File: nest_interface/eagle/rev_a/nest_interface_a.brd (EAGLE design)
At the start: 50.8 x 50.8 mm, 87 parts, among them J1 MOLEX_MICRO_USB_B_047346, J10 CONN_BLOCK_2, J11 CONN_BLOCK_2, J12 CONN_BLOCK_2, J13 CONN_BLOCK_2, J14 CONN_BLOCK_2, J15 CONN_BLOCK_2, J2 CONN_BLOCK_2, J3 CONN_BLOCK_3, J4 PJ-036A-SMT, J5 CONN_BLOCK_3, J6 CONN_BLOCK_3, J7 CONN_BLOCK_2, J8 CONN_BLOCK_3, J9 CONN_BLOCK_3, U1 FT232RL, U2 EPIC-CORE_A

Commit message: started routing the nest interface board
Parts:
- added JP1: (no value), pinhead:2X10
- moved R13 349.9 mm to (45.7, 50.8), turned to 180 degrees
- moved R12 337.4 mm to (45.7, 34.3), turned to 180 degrees
- moved C11 336.6 mm to (45.7, 47.0), turned to 180 degrees
- moved RE6 324.6 mm to (27.9, 45.7)
- moved C10 322.9 mm to (45.7, 30.5), turned to 180 degrees
- moved C9 302.6 mm to (45.7, 12.7), turned to 180 degrees
- moved RE5 292.7 mm to (27.9, 29.2)
- moved R11 291.5 mm to (45.7, 16.5), turned to 180 degrees
- moved RE4 260.2 mm to (27.9, 11.4)
- moved U2 178.7 mm to (74.9, 26.7), turned to 270 degrees
- moved J1 155.3 mm to (58.4, 55.9)
- moved J4 25.4 mm to (17.1, 69.2)
- moved J2 14.0 mm to (3.81, 52.1)
- moved J3 12.7 mm to (3.81, 42.5)
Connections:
- new net ADC5: JP1.1, U2.P$24
- new net ADC6/DAC0: JP1.3, U2.P$25
- new net ADC7/DAC1: JP1.5, U2.P$26
- new net MISO0: JP1.11, U2.P$57
- new net MOSI0/SDA: JP1.9, U2.P$56
- new net P2.0: JP1.2, U2.P$38
- new net P2.1: JP1.4, U2.P$39
- new net P2.3: JP1.6, U2.P$40
- new net P2.6: JP1.8, U2.P$41
- new net RADIO_SFD: JP1.10, U2.P$50
- new net SCLK0/SCL: JP1.13, U2.P$58
- new net STE0: JP1.7, U2.P$55
- new net UART0RX: JP1.17, U2.P$60
- new net UART0TX: JP1.15, U2.P$59
- net FAN_PIN: now also U2.P$31; no longer U2.P$33
- net HEATING_PIN: now also U2.P$33; no longer U2.P$31
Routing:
- net COMMON: track 0.00 -> 71.6 mm
- net W: track 0.00 -> 37.1 mm
- net HEATING_PIN: track 0.00 -> 23.9 mm
- net COOLING_PIN: track 0.00 -> 23.9 mm
- net FAN_PIN: track 0.00 -> 23.9 mm
- net Y: track 0.00 -> 23.7 mm
- net RH: track 0.00 -> 16.5 mm
- net G: track 0.00 -> 12.8 mm
- added copper zone on layer 16, net GND
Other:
- board size 50.8 x 50.8 mm -> 101.6 x 76.2 mm

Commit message: routed the nest interface board
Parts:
- moved J15 472.5 mm to (56.6, 72.4), turned to 180 degrees
- moved J14 467.6 mm to (63.5, 72.4), turned to 180 degrees
- moved JP1 467.1 mm to (64.8, 58.4)
- moved J13 463.7 mm to (72.4, 72.4), turned to 180 degrees
- moved J12 459.2 mm to (79.2, 72.4), turned to 180 degrees
- moved Q8 418.0 mm to (92.7, 30.5), turned to 270 degrees
- moved Q9 412.5 mm to (92.7, 26.2), turned to 270 degrees
- moved Q10 406.9 mm to (92.7, 21.8), turned to 270 degrees
- moved Q6 404.5 mm to (92.7, 40.6), turned to 270 degrees
- moved R23 403.6 mm to (85.9, 30.5), turned to 90 degrees
- moved Q13 403.4 mm to (92.7, 8.89), turned to 270 degrees
- moved Q11 401.3 mm to (92.7, 17.5), turned to 270 degrees
- moved Q5 399.7 mm to (92.7, 45.0), turned to 270 degrees
- moved R29 399.5 mm to (85.9, 17.5), turned to 90 degrees
- moved Q7 398.9 mm to (92.7, 36.3), turned to 270 degrees
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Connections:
- removed net TSTAT1_GND: J7.2
- removed net TSTAT2_GND: J10.2
- net ADC5: now also JP1.16; no longer JP1.1
- net ADC6/DAC0: now also JP1.14; no longer JP1.3
- net ADC7/DAC1: now also JP1.12; no longer JP1.5
- net GND: now also J10.1, J7.1
- net MISO0: now also JP1.13; no longer JP1.11
- net MOSI0/SDA: now also JP1.11; no longer JP1.9
- net P2.0: now also JP1.1; no longer JP1.2
- net P2.1: now also JP1.3; no longer JP1.4
- net P2.3: now also JP1.5; no longer JP1.6
- net P2.6: now also JP1.7; no longer JP1.8
- net SCLK0/SCL: now also JP1.15; no longer JP1.13
- net STE0: now also JP1.9; no longer JP1.7
- net TSTAT1_DOWN: now also J6.1; no longer J6.3
- net TSTAT1_DOWN_PIN: now also U2.P$4; no longer U2.P$7
- net TSTAT1_ENTER: now also J7.2; no longer J7.1
- net TSTAT1_ENTER_PIN: now also U2.P$3; no longer U2.P$8
- net TSTAT1_ESC: now also J6.3; no longer J6.1
- net TSTAT1_ESC_PIN: now also U2.P$6; no longer U2.P$5
- net TSTAT1_HELP_PIN: now also U2.P$5; no longer U2.P$6
- net TSTAT1_MENU_PIN: now also U2.P$8; no longer U2.P$3
- net TSTAT1_ON/OFF: now also J5.3; no longer J5.1
- net TSTAT1_ON/OFF_PIN: now also U2.P$9; no longer U2.P$2
- net TSTAT1_UP: now also J5.1; no longer J5.3
- net TSTAT1_UP_PIN: now also U2.P$7; no longer U2.P$4
- net TSTAT2_DOWN: now also J9.1; no longer J9.3
- net TSTAT2_ENTER: now also J10.2; no longer J10.1
- net TSTAT2_ESC: now also J9.3; no longer J9.1
- net TSTAT2_ON/OFF: now also J8.3; no longer J8.1
- net TSTAT2_ON/OFF_PIN: now also U2.P$2; no longer U2.P$9
- net TSTAT2_UP: now also J8.1; no longer J8.3
- net UART0RX: now also JP1.19; no longer JP1.17
- net UART0TX: now also JP1.17; no longer JP1.15
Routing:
- net VCC: track 0.00 -> 225.6 mm, vias 0 -> 9
- net GND: track 0.00 -> 102.8 mm, vias 0 -> 26
- net N$14: track 0.00 -> 66.3 mm, vias 0 -> 2
- net N$8: track 0.00 -> 65.0 mm
- net TSTAT2_ENTER_PIN: track 0.00 -> 59.0 mm, vias 0 -> 2
- net N$12: track 0.00 -> 56.0 mm, vias 0 -> 2
- net N$9: track 0.00 -> 53.9 mm, vias 0 -> 4
- net TSTAT2_DOWN_PIN: track 0.00 -> 50.9 mm, vias 0 -> 2
- net 5V: track 0.00 -> 49.8 mm
- net TSTAT2_HELP_PIN: track 0.00 -> 46.2 mm, vias 0 -> 2
- net HEATING_PIN: track 23.9 -> 70.0 mm
- net TSTAT2_ESC_PIN: track 0.00 -> 41.3 mm, vias 0 -> 2
- net RADIO_SFD: track 0.00 -> 39.6 mm, vias 0 -> 1
- net UART0RX: track 0.00 -> 37.1 mm, vias 0 -> 1
- net UART0TX: track 0.00 -> 36.6 mm, vias 0 -> 1
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- added copper zone on layer 1, net GND
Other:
- board size 101.6 x 76.2 mm -> 105.4 x 76.2 mm

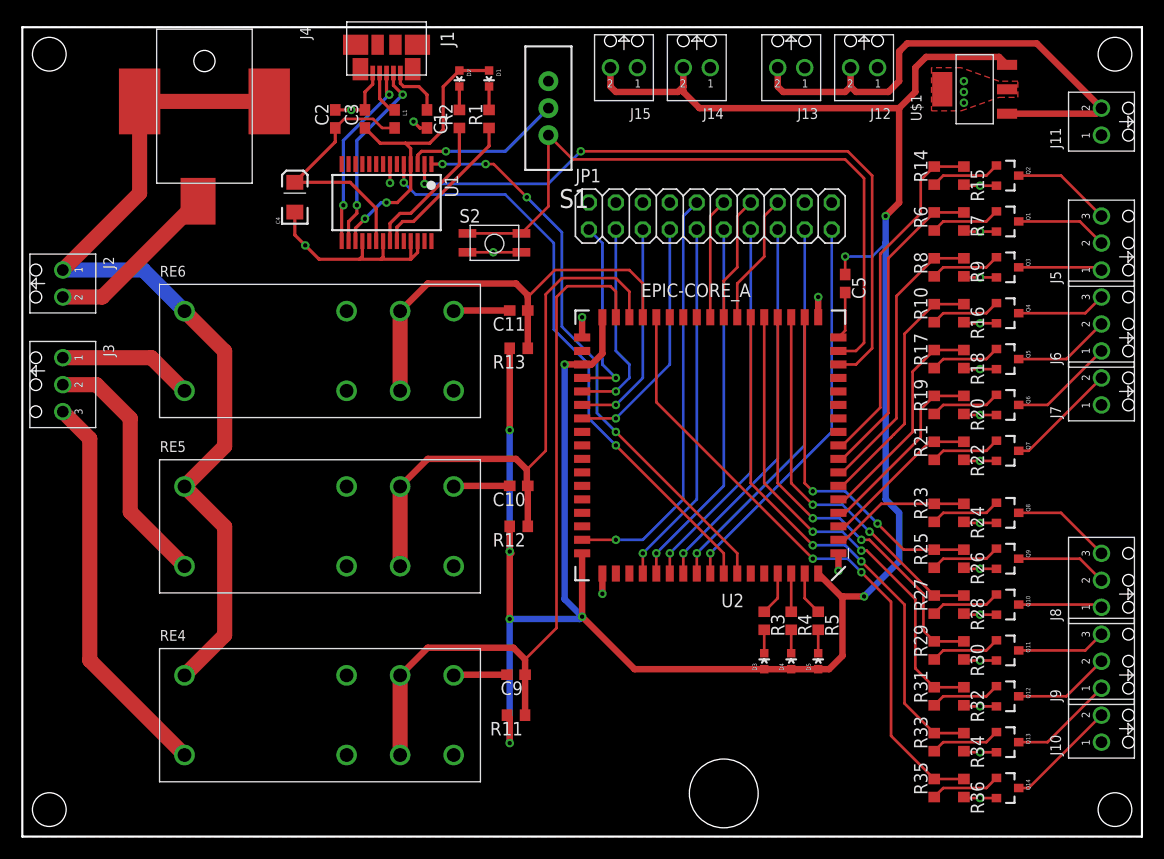
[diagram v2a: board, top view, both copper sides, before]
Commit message: added silkscreen to nest board
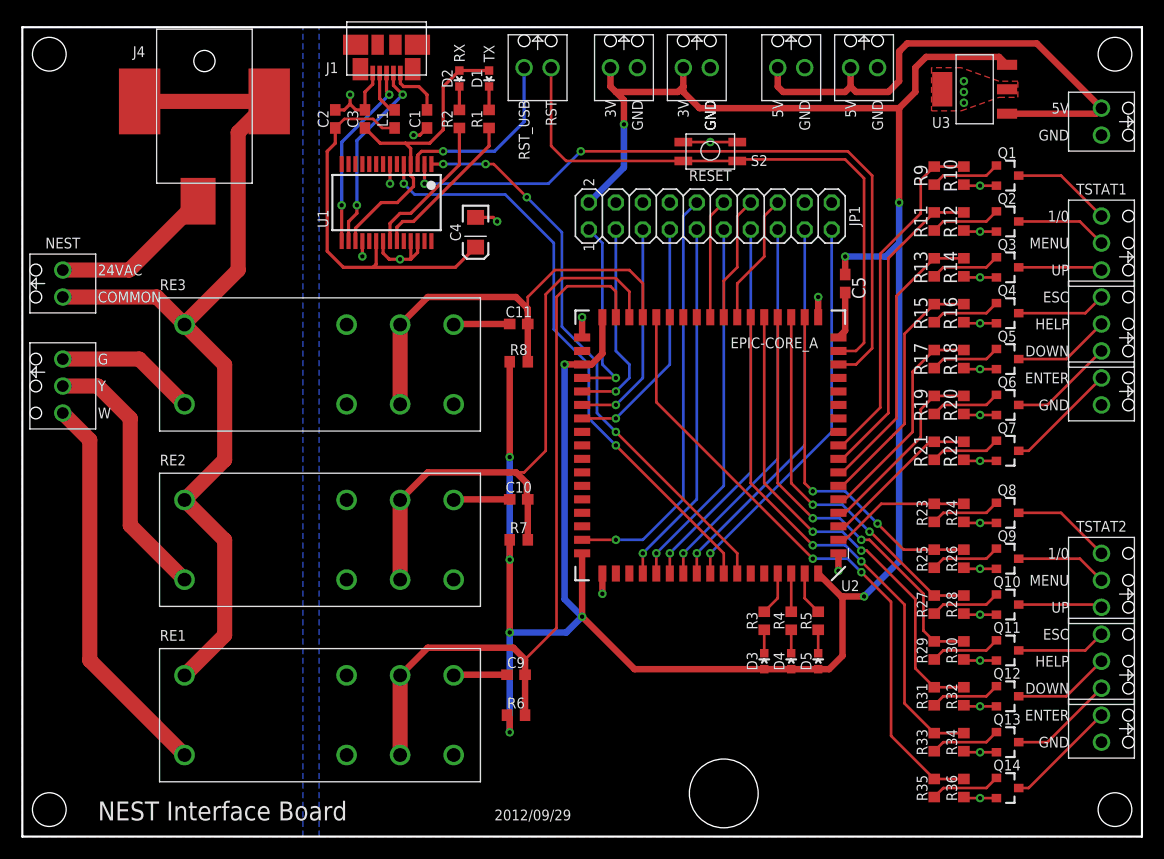
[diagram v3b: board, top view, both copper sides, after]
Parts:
- removed RE5, RE6: RT314524, nest_interface:S0418-CA
- removed S1: (no value), SparkFun:SWITCH-SPDT
- added J16: CONN_BLOCK_2, nest_interface:CONN_BLOCK_2
- added RE2, RE3: RT314524, nest_interface:S0418-CA
- R10, R14, R6, R8: value 10k -> 100k
- R11, R13, R15, R9: value 100k -> 10k
- moved R11 60.9 mm to (85.9, 57.9), turned to 90 degrees
- moved R6 60.9 mm to (46.5, 11.4), turned to 180 degrees
- moved R7 51.5 mm to (46.7, 27.9), turned to 180 degrees
- moved R12 50.8 mm to (88.6, 57.9), turned to 270 degrees
- moved R8 40.1 mm to (46.7, 44.7), turned to 180 degrees
- moved R13 39.9 mm to (85.9, 53.6), turned to 90 degrees
- moved S2 22.1 mm to (64.8, 64.5), turned to 180 degrees
- moved C4 17.3 mm to (42.7, 56.9), turned to 270 degrees
- moved R10 13.3 mm to (88.6, 62.2), turned to 270 degrees
- moved R15 13.3 mm to (85.9, 49.3), turned to 90 degrees
- moved R14 9.08 mm to (88.6, 53.6), turned to 270 degrees
- moved R9 9.08 mm to (85.9, 62.2), turned to 90 degrees
- moved Q1 4.32 mm to (92.7, 62.2)
- moved Q2 4.32 mm to (92.7, 57.9)
- moved C10 1.27 mm to (46.7, 31.8)
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- renumbered RE4 to RE1, U$1 to U3
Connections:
- removed net N$13: S1.2, U1.3
- removed net N$8: S1.1, S2.P$2, S2.P$4, U2.P$16
- new net RST: J16.1, S2.P$2, S2.P$4, U2.P$16
- new net RST_USB: J16.2, U1.3
- net COMMON: now also J2.2, RE2.A2, RE3.A2; no longer J2.1, RE5.A2, RE6.A2
- net COOLING_PIN: now also R7.1, RE2.COMMON1, RE2.COMMON2; no longer R12.1, RE5.COMMON1, RE5.COMMON2
- net FAN_PIN: now also R8.1, RE3.COMMON1, RE3.COMMON2; no longer R13.1, RE6.COMMON1, RE6.COMMON2
- net G: now also RE3.A1; no longer RE6.A1
- net GND: now also JP1.20, R10.2, R12.2, R14.2, RE2.NO1, RE2.NO2, RE3.NO1, RE3.NO2; no longer R15.2, R7.2, R9.2, RE5.NO1, RE5.NO2, RE6.NO1, RE6.NO2
- net HEATING_PIN: now also R6.1; no longer R11.1
- net N$16: now also Q2.1, R11.1; no longer Q1.1, R6.1
- net N$17: now also Q1.1, R9.1; no longer Q2.1, R14.1
- net N$25: now also R13.1; no longer R8.1
- net N$26: now also R15.1; no longer R10.1
- net RH: now also J2.1; no longer J2.2
- net TSTAT1_ESC_PIN: now also R15.2; no longer R10.2
- net TSTAT1_MENU: now also Q2.3; no longer Q1.3
- net TSTAT1_MENU_PIN: now also R11.2, R12.1; no longer R6.2, R7.1
- net TSTAT1_ON/OFF: now also Q1.3; no longer Q2.3
- net TSTAT1_ON/OFF_PIN: now also R10.1, R9.2; no longer R14.2, R15.1
- net TSTAT1_UP_PIN: now also R13.2, R14.1; no longer R8.2, R9.1
- net VCC: now also JP1.2, R6.2, R7.2, R8.2; no longer R11.2, R12.2, R13.2
- net Y: now also RE2.A1; no longer RE5.A1
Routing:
- net N$8: track 65.0 -> 0.00 mm
- net RST: track 0.00 -> 56.4 mm
- net RST_USB: track 0.00 -> 17.2 mm, vias 0 -> 1
- net N$13: track 15.0 -> 0.00 mm, vias 1 -> 0
- net N$6: track 24.7 -> 36.2 mm
- net VCC: track 225.6 -> 234.4 mm, vias 9 -> 10
- net GND: track 102.8 -> 94.2 mm, vias 26 -> 28
- net COMMON: track 84.7 -> 88.3 mm
- net COOLING_PIN: track 55.0 -> 56.9 mm
- net FAN_PIN: track 41.6 -> 42.9 mm
- net Y: track 23.7 -> 24.9 mm
- net RH: track 16.5 -> 15.4 mm
- net N$15: track 30.0 -> 30.2 mm, vias 2 -> 0
- added copper zone on layer 16, net N$37
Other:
- board text added: "1"
- board text added: "1/0"
- board text added: "2"
- board text added: "2012/09/29"
- board text added: "24VAC"
- board text added: "3V"
- board text added: "5V"
- board text added: "COMMON"
- board text added: "DOWN"
- board text added: "ENTER"
- board text added: "ESC"
- board text added: "G"
- board text added: "GND"
- board text added: "HELP"
- board text added: "MENU"
- board text added: "NEST"
- board text added: "NEST Interface Board"
- board text added: "RESET"
- board text added: "RST"
- board text added: "RST_USB"
- board text added: "RX"
- board text added: "TSTAT1"
- board text added: "TSTAT2"
- board text added: "TX"
- board text added: "UP"
- board text added: "W"
- board text added: "Y"

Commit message: tweaks to nest interface board
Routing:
- net GND: vias 28 -> 30
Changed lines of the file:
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@@
 <wire x1="88.746" y1="3.622" x2="90.17" y2="3.622" width="0.254" layer="1"/>
 <polygon width="0.254" layer="1">
-<vertex x="85.598" y="72.39"/>
-<vertex x="85.598" y="68.326"/>
+<vertex x="85.09" y="72.39"/>
+<vertex x="85.09" y="68.326"/>
 <vertex x="88.392" y="68.326"/>
-<vertex x="91.948" y="69.596"/>
-<vertex x="93.726" y="69.596"/>
-<vertex x="93.726" y="71.12"/>
-<vertex x="91.948" y="71.12"/>
+<vertex x="91.948" y="68.834"/>
+<vertex x="94.234" y="68.834"/>
+<vertex x="94.234" y="71.882"/>
+<vertex x="91.948" y="71.882"/>
 <vertex x="88.392" y="72.39"/>
 </polygon>
-<via x="88.646" y="71.12" extent="1-16" drill="0.4064"/>
-<via x="88.646" y="70.104" extent="1-16" drill="0.4064"/>
-<via x="88.646" y="69.088" extent="1-16" drill="0.4064"/>
+<via x="88.646" y="71.374" extent="1-16" drill="0.4064"/>
+<via x="88.646" y="70.358" extent="1-16" drill="0.4064"/>
+<via x="88.646" y="69.342" extent="1-16" drill="0.4064"/>
 <wire x1="54.61" y1="24.765" x2="54.61" y2="22.86" width="0.6096" layer="1"/>
 <via x="54.61" y="22.86" extent="1-16" drill="0.4064"/>
@@
 <wire x1="44.32" y1="58.296" x2="44.704" y2="57.912" width="0.3048" layer="1"/>
 <via x="44.704" y="57.912" extent="1-16" drill="0.4064"/>
+<via x="89.916" y="70.358" extent="1-16" drill="0.4064"/>
+<via x="91.186" y="70.358" extent="1-16" drill="0.4064"/>
 </signal>
 <signal name="N$1">
@@
 <contactref element="J13" pad="2"/>
 <wire x1="101.078" y1="68.058" x2="92.712" y2="68.058" width="0.6096" layer="1"/>
-<wire x1="95.504" y1="74.676" x2="83.312" y2="74.676" width="0.6096" layer="1"/>
 <wire x1="77.978" y1="70.612" x2="77.978" y2="72.39" width="0.6096" layer="1"/>
 <wire x1="71.12" y1="72.39" x2="71.12" y2="70.612" width="0.6096" layer="1"/>
@@
 <wire x1="78.486" y1="70.104" x2="81.534" y2="70.104" width="0.6096" layer="1"/>
 <wire x1="81.534" y1="70.104" x2="82.55" y2="71.12" width="0.6096" layer="1"/>
-<wire x1="82.55" y1="71.12" x2="82.55" y2="73.914" width="0.6096" layer="1"/>
-<wire x1="82.55" y1="73.914" x2="83.312" y2="74.676" width="0.6096" layer="1"/>
 <wire x1="101.078" y1="68.058" x2="101.6" y2="68.58" width="0.6096" layer="1"/>
-<wire x1="101.6" y1="68.58" x2="95.504" y2="74.676" width="0.6096" layer="1"/>
+<wire x1="101.6" y1="68.58" x2="101.6" y2="70.612" width="0.6096" layer="1"/>
+<wire x1="101.6" y1="70.612" x2="97.536" y2="74.676" width="0.6096" layer="1"/>
+<wire x1="97.536" y1="74.676" x2="84.582" y2="74.676" width="0.6096" layer="1"/>
+<wire x1="84.582" y1="74.676" x2="82.55" y2="72.644" width="0.6096" layer="1"/>
+<wire x1="82.55" y1="72.644" x2="82.55" y2="71.12" width="0.6096" layer="1"/>
 </signal>
 <signal name="TSTAT1_ON/OFF">

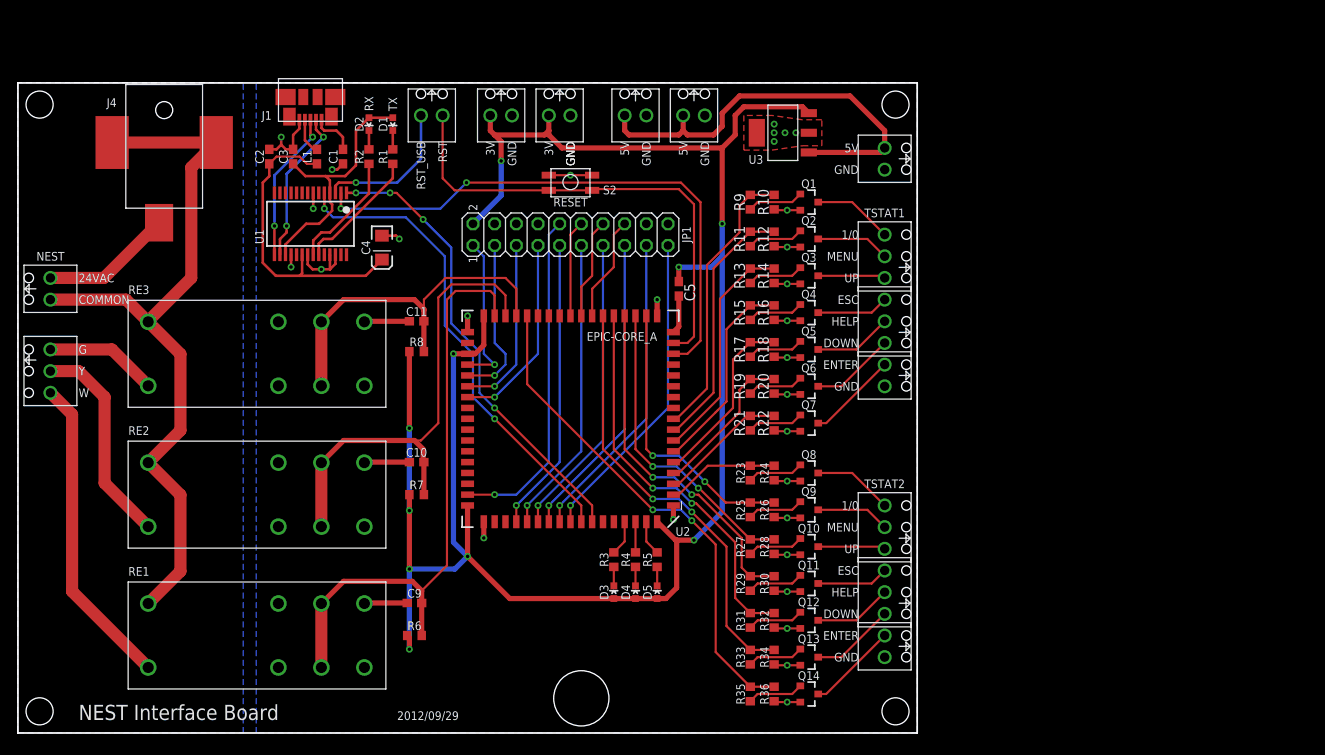
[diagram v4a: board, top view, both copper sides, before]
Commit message: adding more relays to the nest interface board in
prep for v2
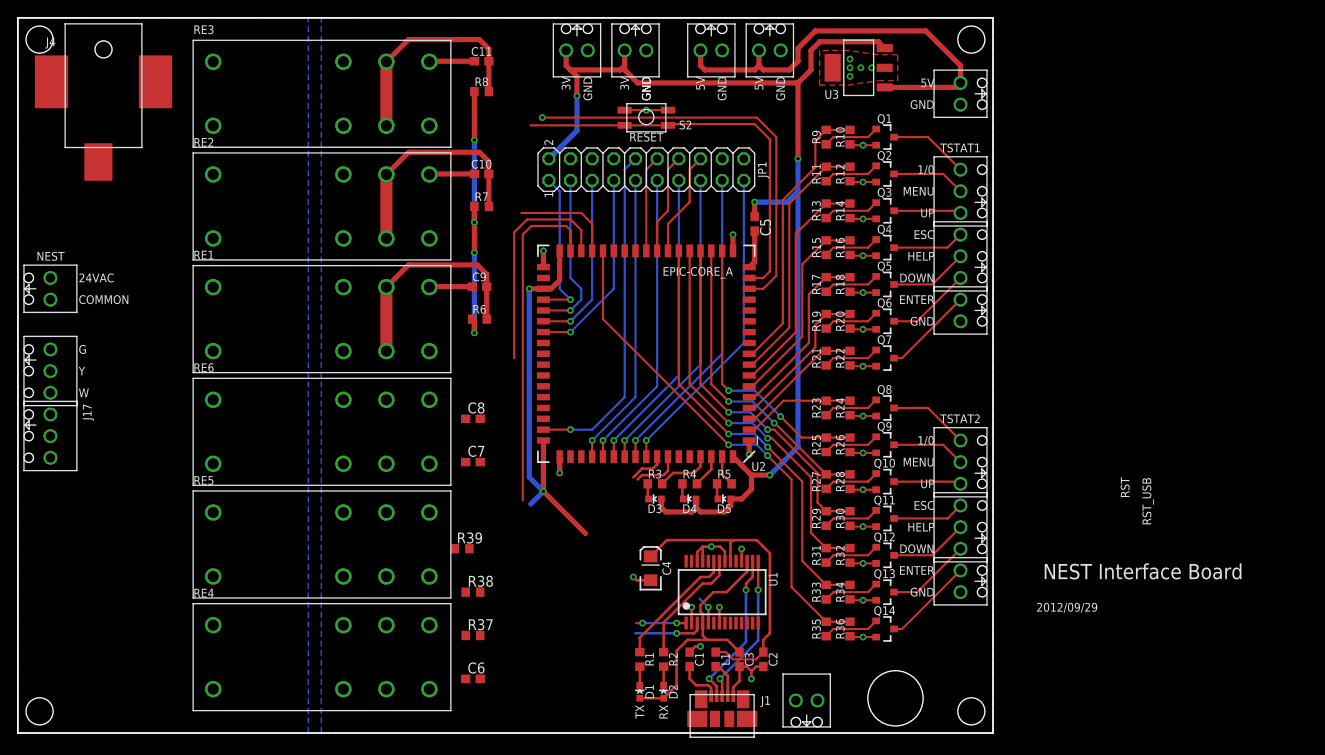
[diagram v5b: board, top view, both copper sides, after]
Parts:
- added C6, C7, C8: (no value), rcl:C0603
- added J17: CONN_BLOCK_3, nest_interface:CONN_BLOCK_3
- added R37, R38, R39: 100k, rcl:R0603
- added RE4, RE5, RE6: RT314524, nest_interface:S0418-CA
- moved J1 87.4 mm to (82.5, 1.65), turned to 90 degrees
- moved C2 82.6 mm to (87.4, 8.64), turned to 270 degrees
- moved J16 81.5 mm to (92.5, 3.81), turned to 0 degrees
- moved C3 78.8 mm to (84.6, 8.64), turned to 270 degrees
- moved L1 75.2 mm to (81.8, 8.64), turned to 90 degrees
- moved D2 75.0 mm to (75.7, 4.83), turned to 0 degrees
- moved D1 72.6 mm to (72.9, 4.83), turned to 0 degrees
- moved C1 71.6 mm to (78.7, 8.64), turned to 90 degrees
- moved R2 68.3 mm to (75.7, 8.64), turned to 270 degrees
- moved R1 65.7 mm to (72.9, 8.64), turned to 270 degrees
- moved U1 64.8 mm to (82.5, 16.5), turned to 0 degrees
- moved C4 49.0 mm to (74.2, 19.3), turned to 90 degrees
- moved RE1 37.9 mm to (35.6, 48.5)
- moved C9 37.9 mm to (54.1, 52.3)
- moved R6 37.9 mm to (54.1, 48.5)
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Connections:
- net COOLING_PIN renamed COOLING1_PIN
- net HEATING_PIN renamed HEATING1_PIN
- net W renamed W1
- net Y renamed Y1
- new net COOLING2_PIN: C7.1, R38.1, RE5.COMMON1, RE5.COMMON2
- new net HEATING2_PIN: C6.1, R37.1, RE4.COMMON1, RE4.COMMON2
- new net STAR: J17.1, RE6.A1
- new net STAR_PIN: C8.1, R39.1, RE6.COMMON1, RE6.COMMON2
- new net W2: J17.3, RE4.A1
- new net Y2: J17.2, RE5.A1
- net COMMON: now also RE4.A2, RE5.A2, RE6.A2
- net GND: now also C6.2, C7.2, C8.2, RE4.NO1, RE4.NO2, RE5.NO1, RE5.NO2, RE6.NO1, RE6.NO2
- net VCC: now also R37.2, R38.2, R39.2
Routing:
- net COMMON: track 88.3 -> 0.00 mm
- net N$12: track 56.0 -> 7.60 mm, vias 2 -> 1
- net N$9: track 53.9 -> 11.5 mm, vias 4 -> 2
- net W1: track 36.9 -> 0.00 mm
- net Y1: track 24.9 -> 0.00 mm
- net VCC: track 234.4 -> 213.2 mm
- net N$14: track 66.3 -> 50.3 mm
- net RH: track 15.4 -> 0.00 mm
- net G: track 13.2 -> 0.00 mm
- net RST: track 56.4 -> 47.1 mm
- net RST_USB: track 17.2 -> 8.22 mm
- net FAN_PIN: track 42.9 -> 38.0 mm
- net COOLING1_PIN: track 56.9 -> 52.5 mm
- net HEATING1_PIN: track 70.0 -> 65.8 mm
- net N$24: track 4.12 -> 6.47 mm
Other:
- board size 105.4 x 76.2 mm -> 114.3 x 83.8 mm
